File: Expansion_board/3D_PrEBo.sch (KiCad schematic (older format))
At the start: 72 parts, among them J1 LED, J10 TMC_INPUT, J11 Power_out, J12 Z_Probe, J13 Fan_interconnection_header, J14 X_MIN, J15 Z_MAX, J2 V_IN, J3 RJ45, J4 X, J5 Y, J6 Z, J7 E0, J8 E1, J9 FAN&LED_INPUT, M1 Fan_3pin, M2 Fan_3pin, M3 Fan_3pin, M4 Fan_3pin, M5 Fan_3pin, M6 Fan_3pin, M7 Fan_3pin, M8 Fan_4pin, Q1 AOD4189, Q10 IRLML2502, Q2 IRLML2502, Q3 IRLML2502, Q4 IRLML2502, Q5 IRLML2502, Q6 IRLML2502, Q7 IRLML2502, Q8 IRLML2502, Q9 IRLML2502, U1 L5973D, U2 NCP1117-5.0_SOT223

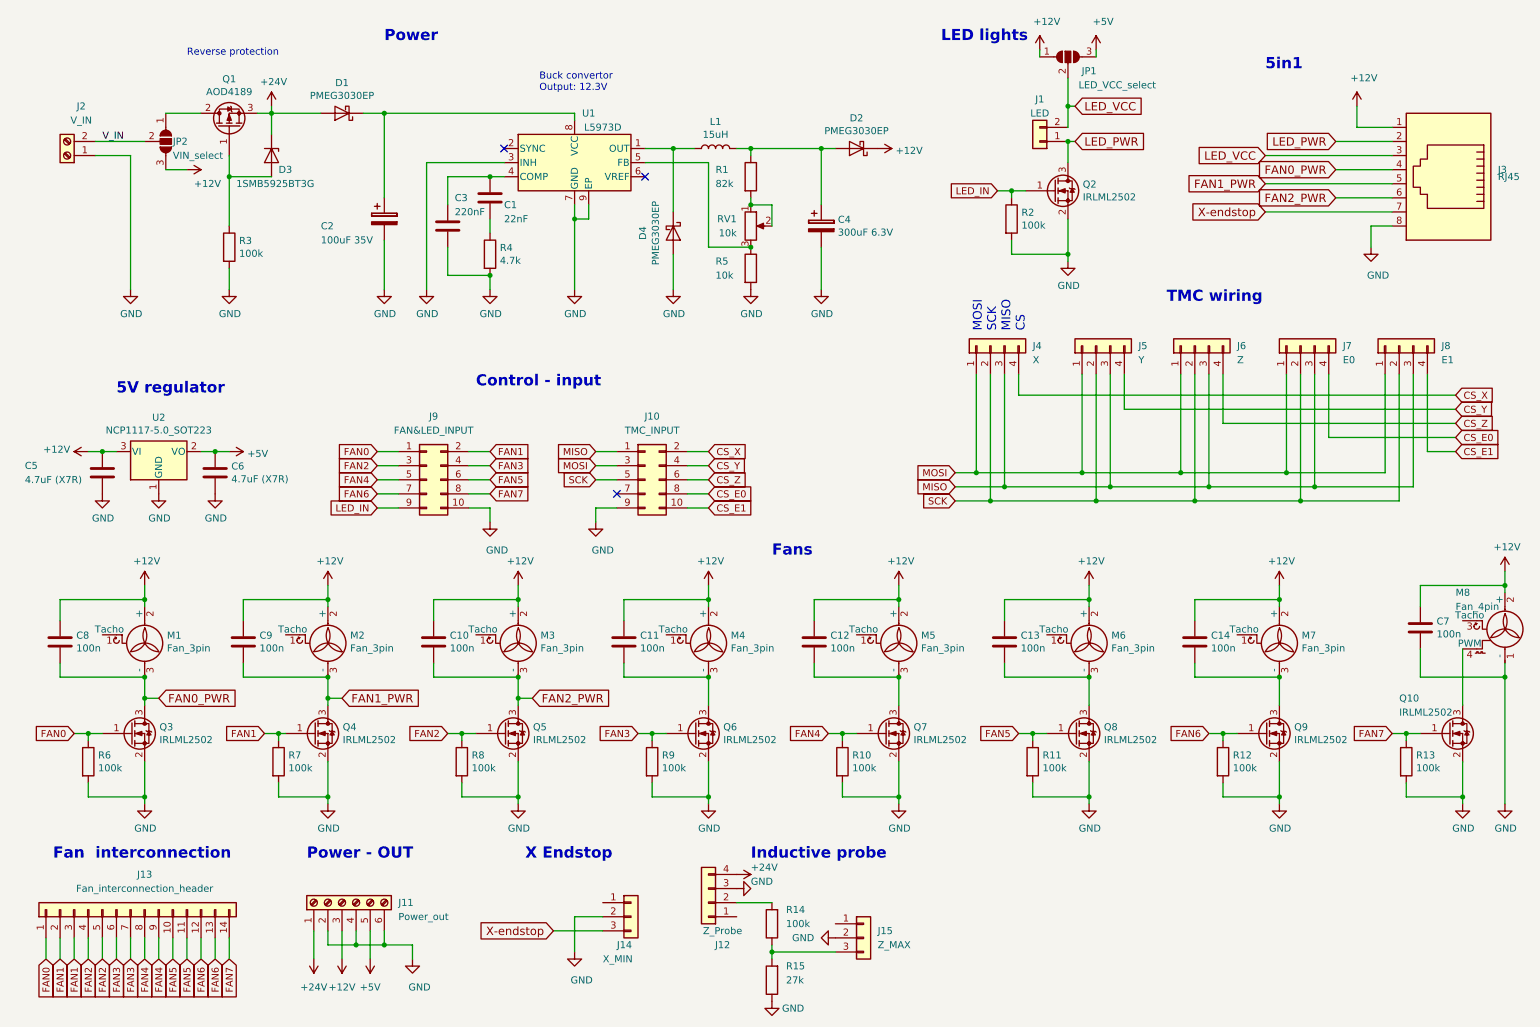
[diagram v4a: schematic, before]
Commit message: Expansiopn_board: PCB: Routing done, Silk screen in progress
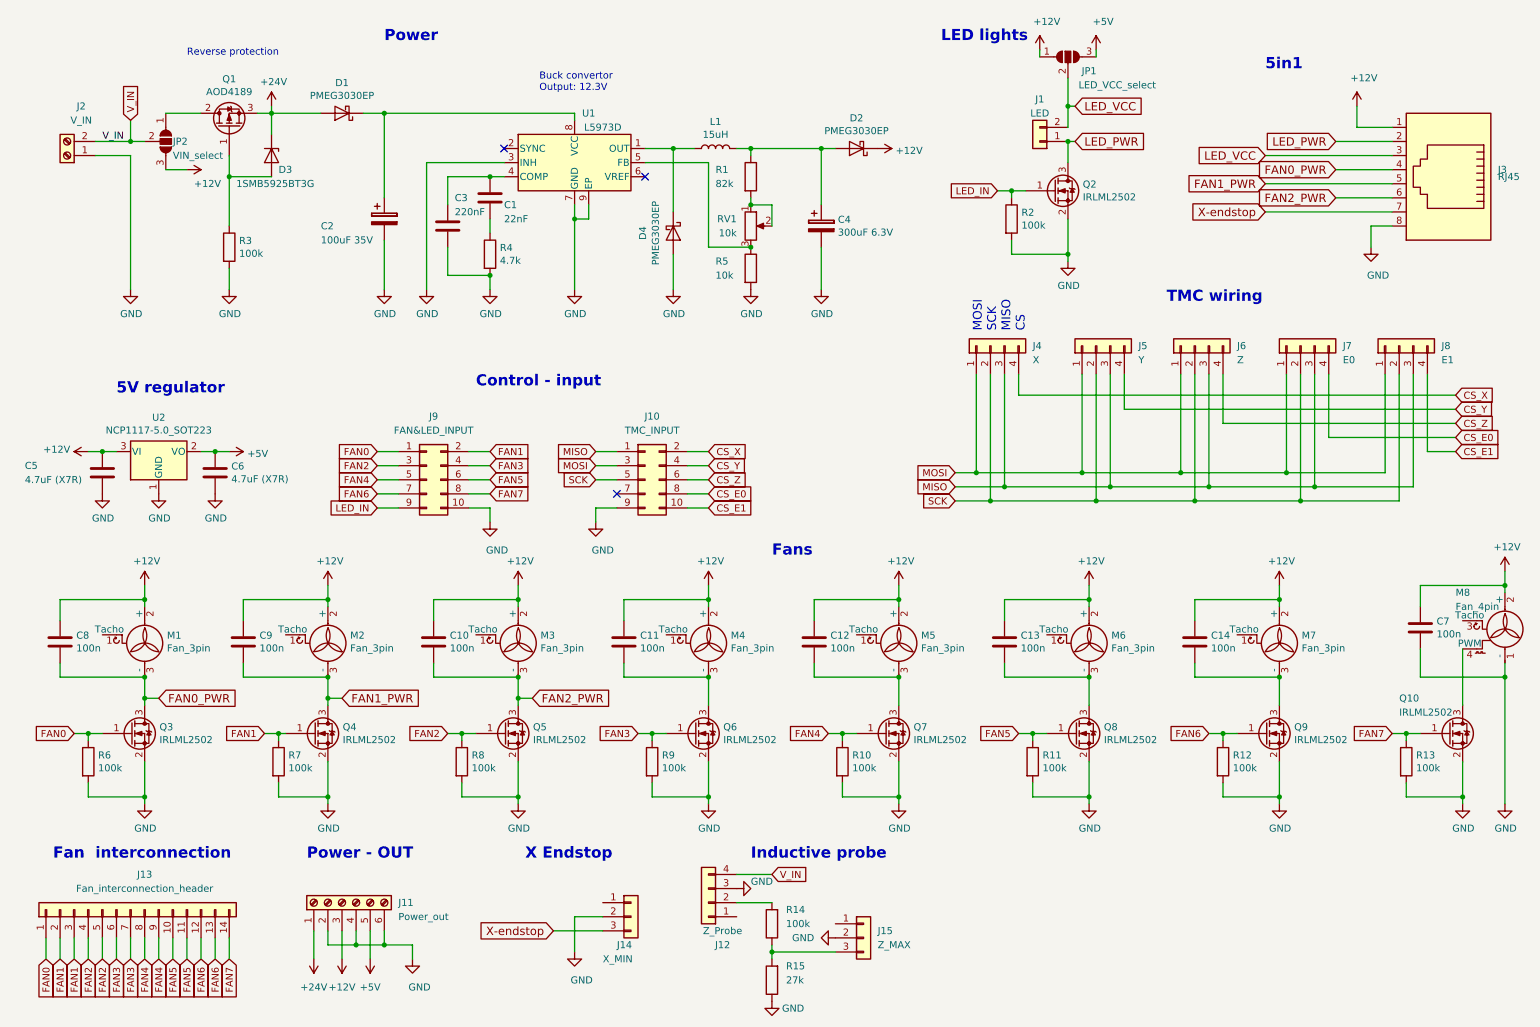
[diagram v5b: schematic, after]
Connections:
- net +24V: no longer J12.4 (Pin_4)
- net V_IN: now also J12.4 (Pin_4)
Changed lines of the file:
@@
 	1250 1600 1250 2550
 Wire Wire Line
-	1000 1500 1350 1500
+	1000 1500 1250 1500
 Wire Wire Line
 	1500 1300 1750 1300
-$Comp
-L power:+24V #PWR042
-U 1 1 5C5C5730
-P 5550 6700
-F 0 "#PWR042" H 5550 6550 50  0001 C CNN
-F 1 "+24V" V 5500 6800 50  0000 L CNN
-F 2 "" H 5550 6700 50  0001 C CNN
-F 3 "" H 5550 6700 50  0001 C CNN
-	1    5550 6700
-	0    1    1    0
-$EndComp
 $Comp
 L power:GND #PWR043
@@
 Wire Wire Line
 	3000 4100 3150 4100
+Text GLabel 5800 6700 2    50   Input ~ 0
+V_IN
+Wire Wire Line
+	5800 6700 5550 6700
+Text GLabel 1250 1350 1    50   Input ~ 0
+V_IN
+Wire Wire Line
+	1250 1350 1250 1500
+Connection ~ 1250 1500
+Wire Wire Line
+	1250 1500 1350 1500
 $EndSCHEMATC

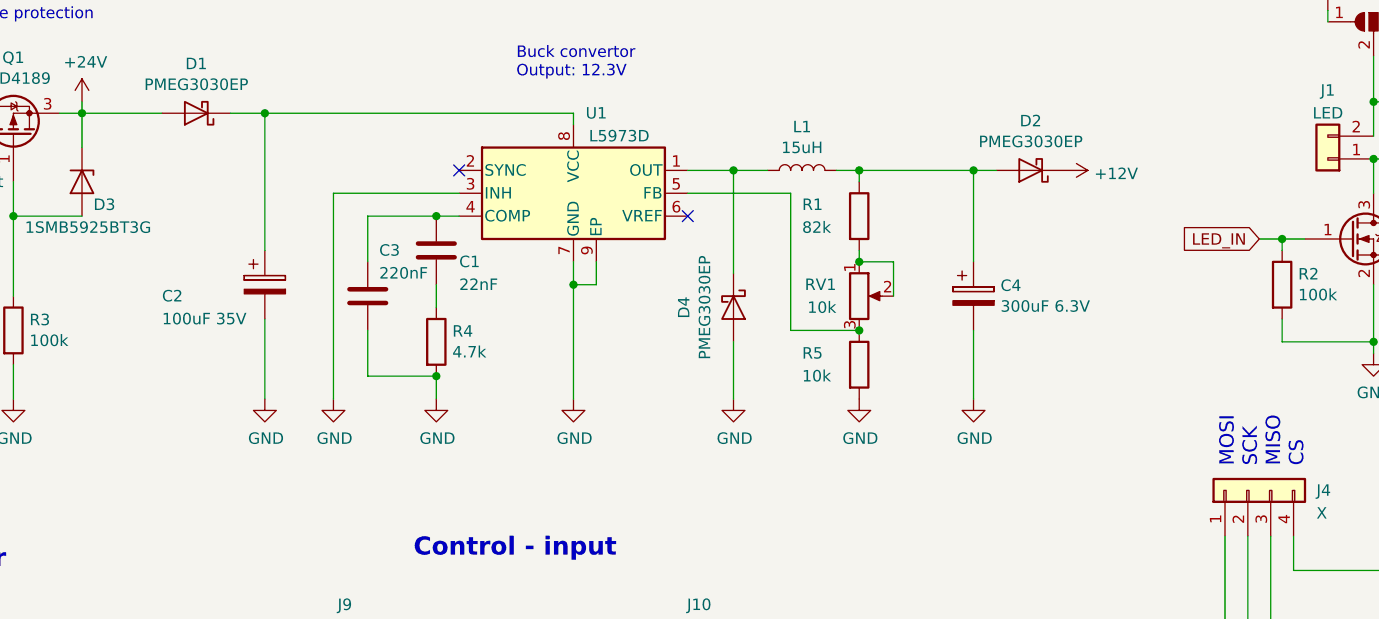
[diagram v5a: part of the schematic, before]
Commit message: Expansion_board: Schema: Change in buck convertor capacitors, add transil
change capacitors to correct packages and voltages
add transil to convertor output as overvoltage protection
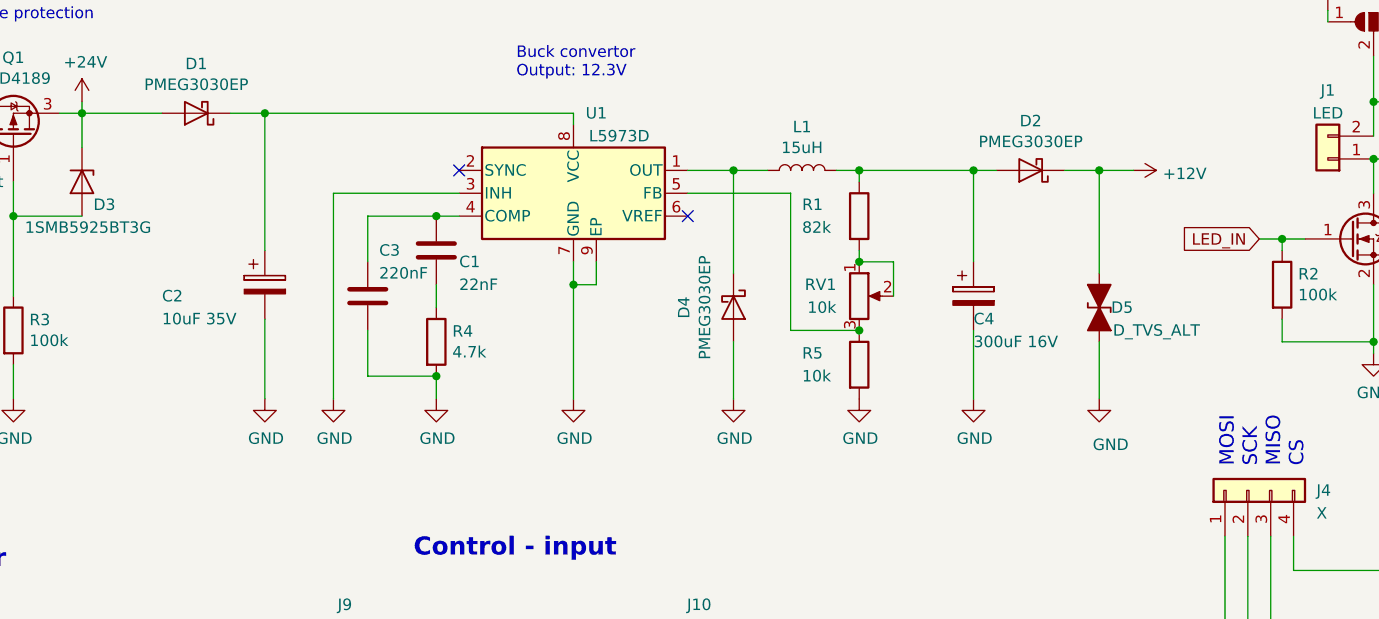
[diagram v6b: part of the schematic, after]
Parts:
- added D5: D_TVS_ALT, Diode_SMD:D_SMA, symbol Device:D_TVS_ALT
- C2: value 100uF 35V -> 10uF 35V; footprint Capacitor_SMD:CP_Elec_6.3x7.7 -> Capacitor_SMD:C_2816_7142Metric_Pad3.20x4.45mm_HandSolder
- C4: value 300uF 6.3V -> 300uF 16V; footprint Capacitor_SMD:CP_Elec_6.3x7.7 -> Capacitor_SMD:CP_Elec_8x10.5
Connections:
- net +12V: now also D5.2 (A2)
- net GND: now also D5.1 (A1)
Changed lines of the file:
@@
 P 3050 2050
 F 0 "C2" H 2600 2000 50  0000 L CNN
-F 1 "100uF 35V" H 2600 1900 50  0000 L CNN
-F 2 "Capacitor_SMD:CP_Elec_6.3x7.7" H 3088 1900 50  0001 C CNN
+F 1 "10uF 35V" H 2600 1900 50  0000 L CNN
+F 2 "Capacitor_SMD:C_2816_7142Metric_Pad3.20x4.45mm_HandSolder" H 3088 1900 50  0001 C CNN
 F 3 "~" H 3050 2050 50  0001 C CNN
 	1    3050 2050
@@
 U 1 1 5C5AC000
 P 6150 2100
-F 0 "C4" H 6268 2146 50  0000 L CNN
-F 1 "300uF 6.3V" H 6268 2055 50  0000 L CNN
-F 2 "Capacitor_SMD:CP_Elec_6.3x7.7" H 6188 1950 50  0001 C CNN
+F 0 "C4" H 6150 2000 50  0000 L CNN
+F 1 "300uF 16V" H 6150 1900 50  0000 L CNN
+F 2 "Capacitor_SMD:CP_Elec_8x10.5" H 6188 1950 50  0001 C CNN
 F 3 "~" H 6150 2100 50  0001 C CNN
 	1    6150 2100
@@
 L power:+12V #PWR05
 U 1 1 5C5C9F90
-P 6550 1550
-F 0 "#PWR05" H 6550 1400 50  0001 C CNN
-F 1 "+12V" V 6565 1678 50  0000 L CNN
-F 2 "" H 6550 1550 50  0001 C CNN
-F 3 "" H 6550 1550 50  0001 C CNN
-	1    6550 1550
+P 6850 1550
+F 0 "#PWR05" H 6850 1400 50  0001 C CNN
+F 1 "+12V" V 6865 1678 50  0000 L CNN
+F 2 "" H 6850 1550 50  0001 C CNN
+F 3 "" H 6850 1550 50  0001 C CNN
+	1    6850 1550
 	0    1    1    0
 $EndComp
@@
 Wire Wire Line
 	1250 1500 1350 1500
+$Comp
+L Device:D_TVS_ALT D5
+U 1 1 5C637E84
+P 6700 2150
+F 0 "D5" V 6700 2050 50  0000 C CNN
+F 1 "D_TVS_ALT" V 6600 1900 50  0000 C CNN
+F 2 "Diode_SMD:D_SMA" H 6700 2150 50  0001 C CNN
+F 3 "~" H 6700 2150 50  0001 C CNN
+	1    6700 2150
+	0    -1   -1   0
+$EndComp
+Wire Wire Line
+	6700 2000 6700 1550
+Wire Wire Line
+	6550 1550 6700 1550
+Connection ~ 6700 1550
+Wire Wire Line
+	6700 1550 6850 1550
+Wire Wire Line
+	6700 2300 6700 2550
+$Comp
+L power:GND #PWR0101
+U 1 1 5C6A962E
+P 6700 2550
+F 0 "#PWR0101" H 6700 2300 50  0001 C CNN
+F 1 "GND" H 6750 2350 50  0000 C CNN
+F 2 "" H 6700 2550 50  0001 C CNN
+F 3 "" H 6700 2550 50  0001 C CNN
+	1    6700 2550
+	1    0    0    -1
+$EndComp
 $EndSCHEMATC

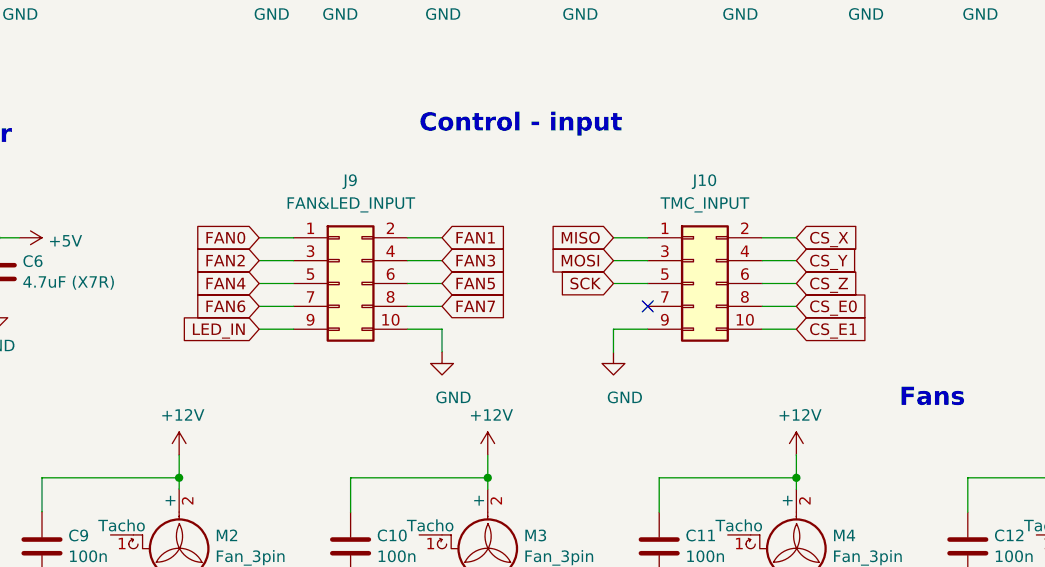
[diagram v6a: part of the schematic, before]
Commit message: Expansion_board: PCB: Add trnasil, reroute capacitors
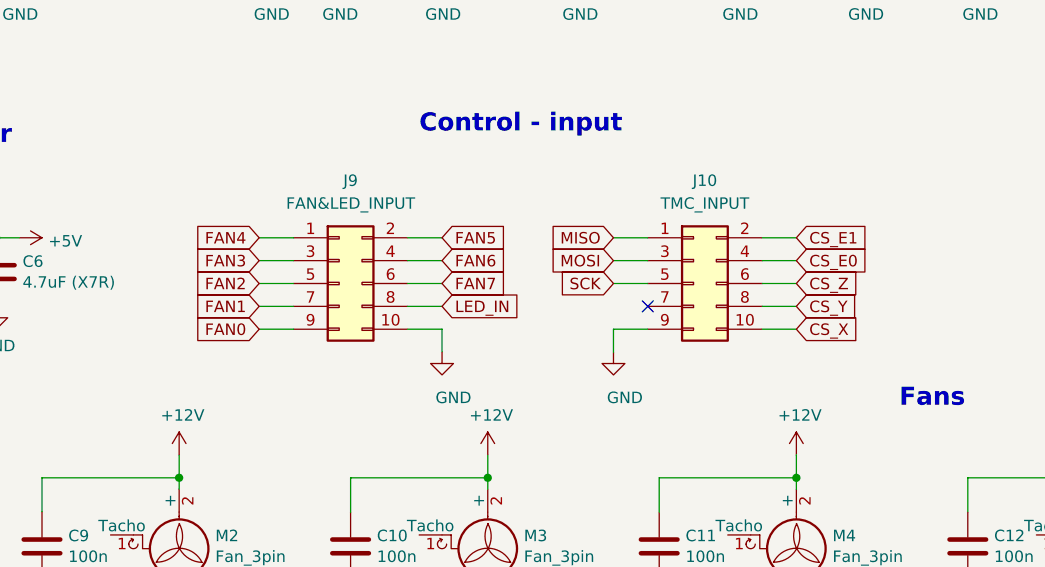
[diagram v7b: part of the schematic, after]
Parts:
- L1: footprint Inductor_SMD:L_Bourns_SRR1260 -> Inductor_SMD:L_Neosid_Ms85
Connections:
- net CS_E0: now also J10.4 (Pin_4); no longer J10.8 (Pin_8)
- net CS_E1: now also J10.2 (Pin_2); no longer J10.10 (Pin_10)
- net CS_X: now also J10.10 (Pin_10); no longer J10.2 (Pin_2)
- net CS_Y: now also J10.8 (Pin_8); no longer J10.4 (Pin_4)
- net FAN0: now also J9.9 (Pin_9); no longer J9.1 (Pin_1)
- net FAN1: now also J9.7 (Pin_7); no longer J9.2 (Pin_2)
- net FAN2: now also J9.5 (Pin_5); no longer J9.3 (Pin_3)
- net FAN3: now also J9.3 (Pin_3); no longer J9.4 (Pin_4)
- net FAN4: now also J9.1 (Pin_1); no longer J9.5 (Pin_5)
- net FAN5: now also J9.2 (Pin_2); no longer J9.6 (Pin_6)
- net FAN6: now also J9.4 (Pin_4); no longer J9.7 (Pin_7)
- net FAN7: now also J9.6 (Pin_6); no longer J9.8 (Pin_8)
- net LED_IN: now also J9.8 (Pin_8); no longer J9.9 (Pin_9)
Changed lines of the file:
@@
 F 0 "L1" V 5590 1550 50  0000 C CNN
 F 1 "15uH" V 5499 1550 50  0000 C CNN
-F 2 "Inductor_SMD:L_Bourns_SRR1260" H 5400 1550 50  0001 C CNN
+F 2 "Inductor_SMD:L_Neosid_Ms85" H 5400 1550 50  0001 C CNN
 F 3 "~" H 5400 1550 50  0001 C CNN
 	1    5400 1550
@@
 Wire Wire Line
 	4250 7100 4600 7100
+Text GLabel 3000 4100 0    50   Input ~ 0
+FAN0
+Text GLabel 3000 4000 0    50   Input ~ 0
+FAN1
+Wire Wire Line
+	3000 3700 3150 3700
+Wire Wire Line
+	3650 3700 3800 3700
+Text GLabel 3000 3900 0    50   Input ~ 0
+FAN2
+Text GLabel 3000 3800 0    50   Input ~ 0
+FAN3
 Text GLabel 3000 3700 0    50   Input ~ 0
-FAN0
+FAN4
 Text GLabel 3800 3700 2    50   Input ~ 0
-FAN1
-Wire Wire Line
-	3000 3700 3150 3700
-Wire Wire Line
-	3650 3700 3800 3700
-Text GLabel 3000 3800 0    50   Input ~ 0
-FAN2
+FAN5
 Text GLabel 3800 3800 2    50   Input ~ 0
-FAN3
-Text GLabel 3000 3900 0    50   Input ~ 0
-FAN4
+FAN6
 Text GLabel 3800 3900 2    50   Input ~ 0
-FAN5
-Text GLabel 3000 4000 0    50   Input ~ 0
-FAN6
-Text GLabel 3800 4000 2    50   Input ~ 0
 FAN7
 $Comp
@@
 Wire Wire Line
 	4700 4100 4550 4100
-Text GLabel 5350 3700 2    50   Input ~ 0
+Text GLabel 5350 4100 2    50   Input ~ 0
 CS_X
-Text GLabel 5350 3800 2    50   Input ~ 0
+Text GLabel 5350 4000 2    50   Input ~ 0
 CS_Y
 Text GLabel 5350 3900 2    50   Input ~ 0
 CS_Z
-Text GLabel 5350 4000 2    50   Input ~ 0
+Text GLabel 5350 3800 2    50   Input ~ 0
 CS_E0
-Text GLabel 5350 4100 2    50   Input ~ 0
+Text GLabel 5350 3700 2    50   Input ~ 0
 CS_E1
 Wire Wire Line
@@
 	5800 1950 5800 2100
 Connection ~ 5650 1950
-Text GLabel 3000 4100 0    50   Input ~ 0
+Text GLabel 3800 4000 2    50   Input ~ 0
 LED_IN
 Wire Wire Line
